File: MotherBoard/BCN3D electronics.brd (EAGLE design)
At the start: 80 x 140 mm, 200 parts, among them IC1 LM358D, IC2 FT232RL, IC3 LM311D, K1 G5L, Q1 MOSFET-NSOIC8, Q2 MOSFET-NSOIC8, Q3 MOSFET-NSOIC8, Q4 MMBT2222A, Q5 MMBT2222A, Q9 MMBT2222A, U1 INA169, X0 FFC_15V_90G_1MM, X1 FFC_15V_90G_1MM, Y0 FFC_15V_90G_1MM

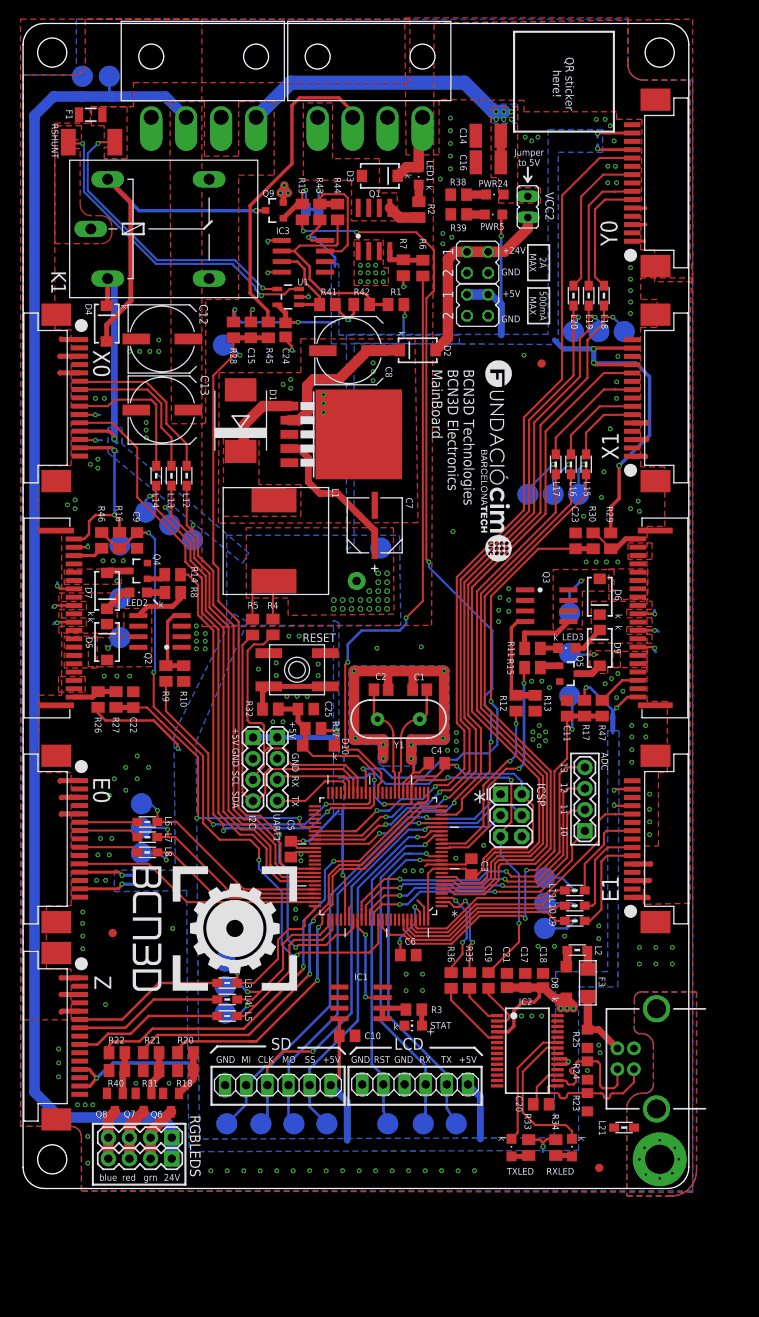
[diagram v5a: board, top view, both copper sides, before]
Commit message: Fixed thermistor series resistors
Added new license info and WEEE/FCC/CE Logo.
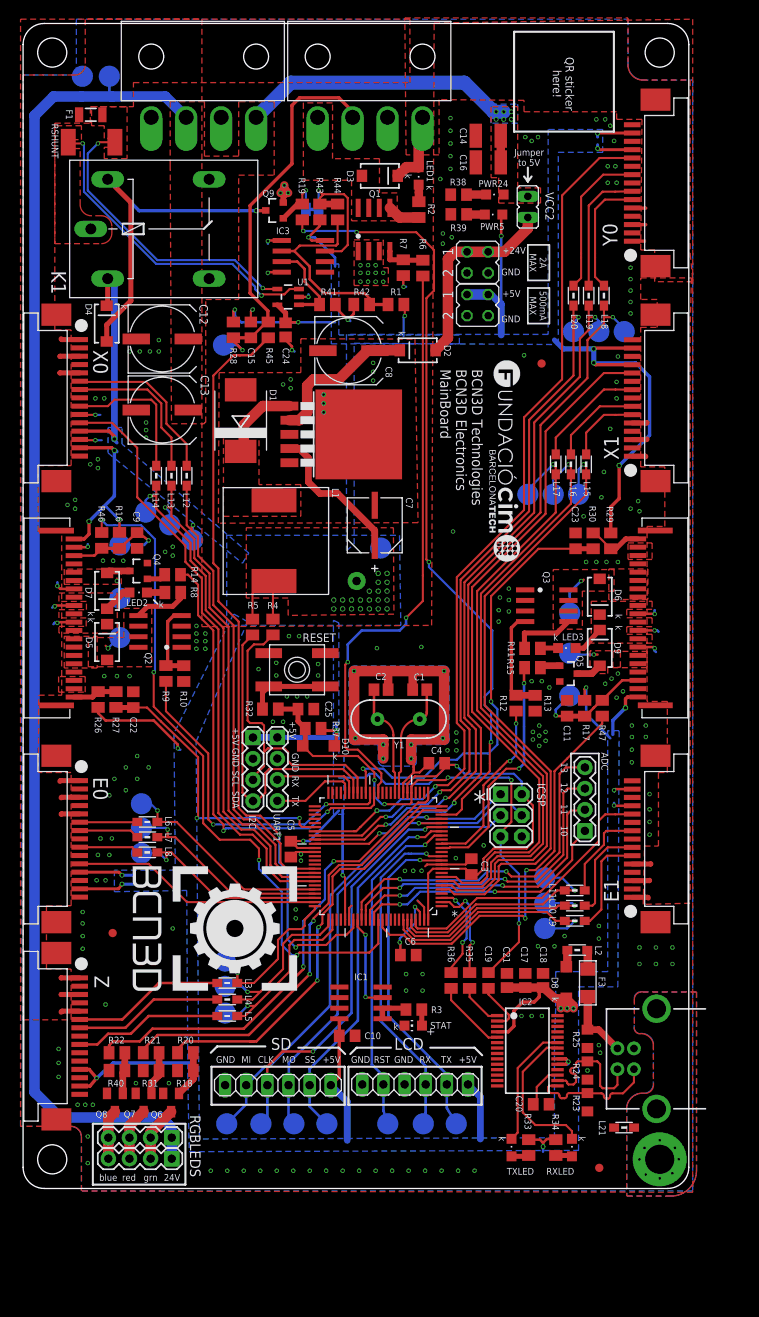
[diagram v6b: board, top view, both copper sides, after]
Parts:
- removed U$1: (no value), MarcEagleParts:BCN3D_QR
- removed U$7: (no value), MarcEagleParts:CC_LOGO
- added U$2: (no value), logo:TONNE_10.00
- added U$3: (no value), logo:FCC_10X4.175MM
- added U$4: (no value), logo:CE-4MM
- moved LOGO1 1.68 mm to (24.7, 90.6)
- moved U$9 1.00 mm to (52.4, 101.3)
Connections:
- net BED_THERM: no longer C15.1, R28.1, TP13.TP
- net BED_THERM_CON: now also C15.1, R28.1, TP13.TP
- net HOTEND0_THERM: no longer C9.1, R16.1, TP12.TP
- net HOTEND0_THERM_CON: now also C9.1, R16.1, TP12.TP
- net HOTEND1_THERM: no longer C11.1, R17.1, TP11.TP
- net HOTEND1_THERM_CON: now also C11.1, R17.1, TP11.TP
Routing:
- net HOTEND0_THERM_CON: track 3.69 -> 14.1 mm, vias 0 -> 1
- net BED_THERM_CON: track 38.1 -> 47.5 mm, vias 0 -> 1
- net HOTEND1_THERM_CON: track 5.27 -> 14.7 mm, vias 0 -> 1
- net HOTEND1_THERM: track 56.9 -> 49.2 mm, vias 3 -> 2
- net BED_THERM: track 95.7 -> 91.2 mm, vias 3 -> 2
- net HOTEND0_THERM: track 85.1 -> 81.7 mm
- net +5V: track 393.5 -> 396.3 mm, vias 52 -> 53
- net GND: vias 234 -> 237
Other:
- board text added: "BCN3D Technologies BCN3D Electronics MainBoard v1.0 Designed in Barcelona ___________________ Sep 2015 - REV_F"
- board text added: "Released under CERN-OHL"
- board text removed: "BCN3D Technologies BCN3D Electronics MainBoard v1.0 Designed in Barcelona ___________________ Sep 2015 - REV_E"
- board text removed: "For more info scan QR Code"

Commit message: Motherboard updated to new version REV.G
Basically the only change in REV.G is the 20 contacts Flat Flexible
Cable connector.
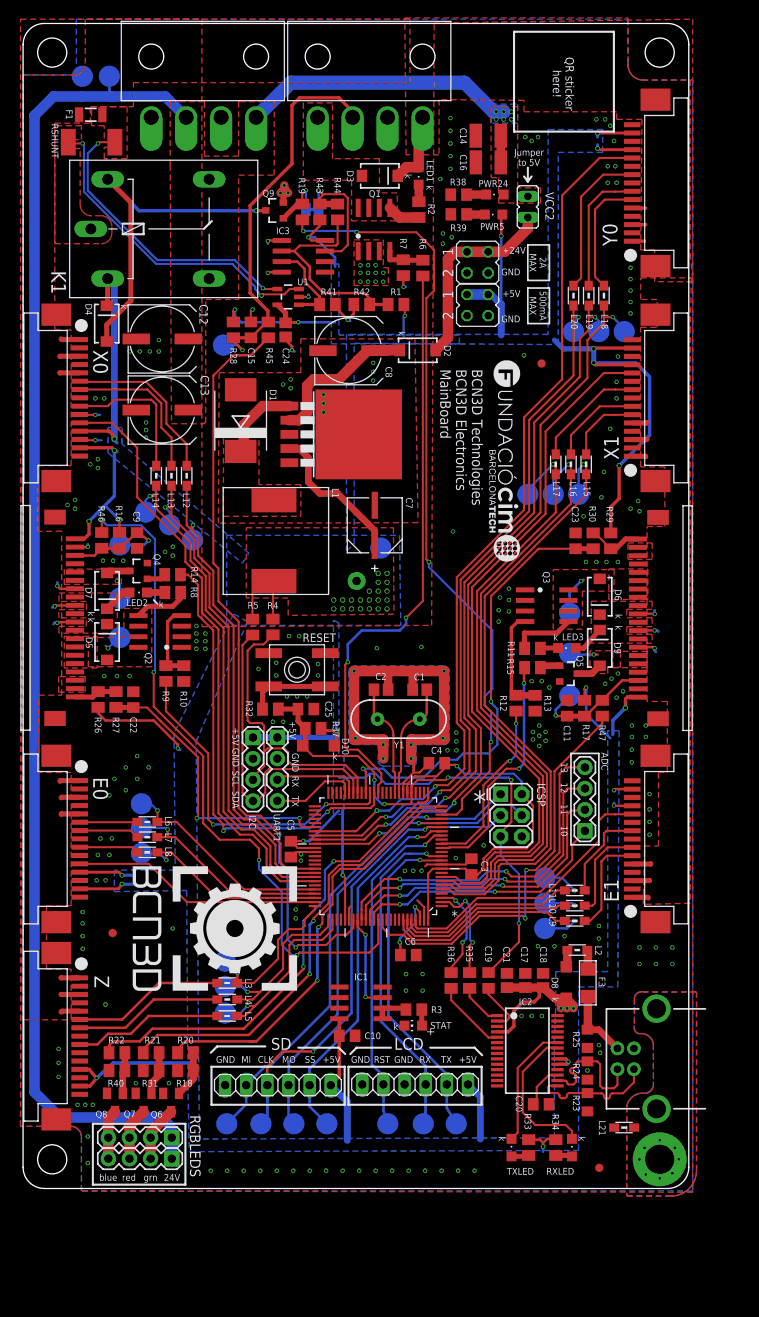
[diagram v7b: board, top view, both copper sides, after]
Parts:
- HOTEND0, HOTEND1: value FFC_20V_90G_1MM3 -> 68612014422; device MarcEagleParts:FCI_20WAY_1MM_3ST -> FPC_FFC_Connectors_:68612014422
- moved HOTEND0 6.43 mm to (5.14, 62.3)
- moved HOTEND1 6.40 mm to (75.0, 74.8)
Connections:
- net GND: no longer HOTEND0.GND1, HOTEND0.GND2, HOTEND1.GND1, HOTEND1.GND2
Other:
- board text added: "BCN3D Technologies BCN3D Electronics MainBoard v1.0 Designed in Barcelona ___________________ Oct 2016 - REV_G"
- board text removed: "BCN3D Technologies BCN3D Electronics MainBoard v1.0 Designed in Barcelona ___________________ Sep 2015 - REV_F"
